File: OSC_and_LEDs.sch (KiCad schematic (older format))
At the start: 49 parts, among them Q2 IRLML2502, Q3 IRLML2502, Q4 IRLML2502, Q5 IRLML2502, Q6 IRLML2502, Q7 IRLML2502, U1 xc7a50tftg256, X1 ASFLMB

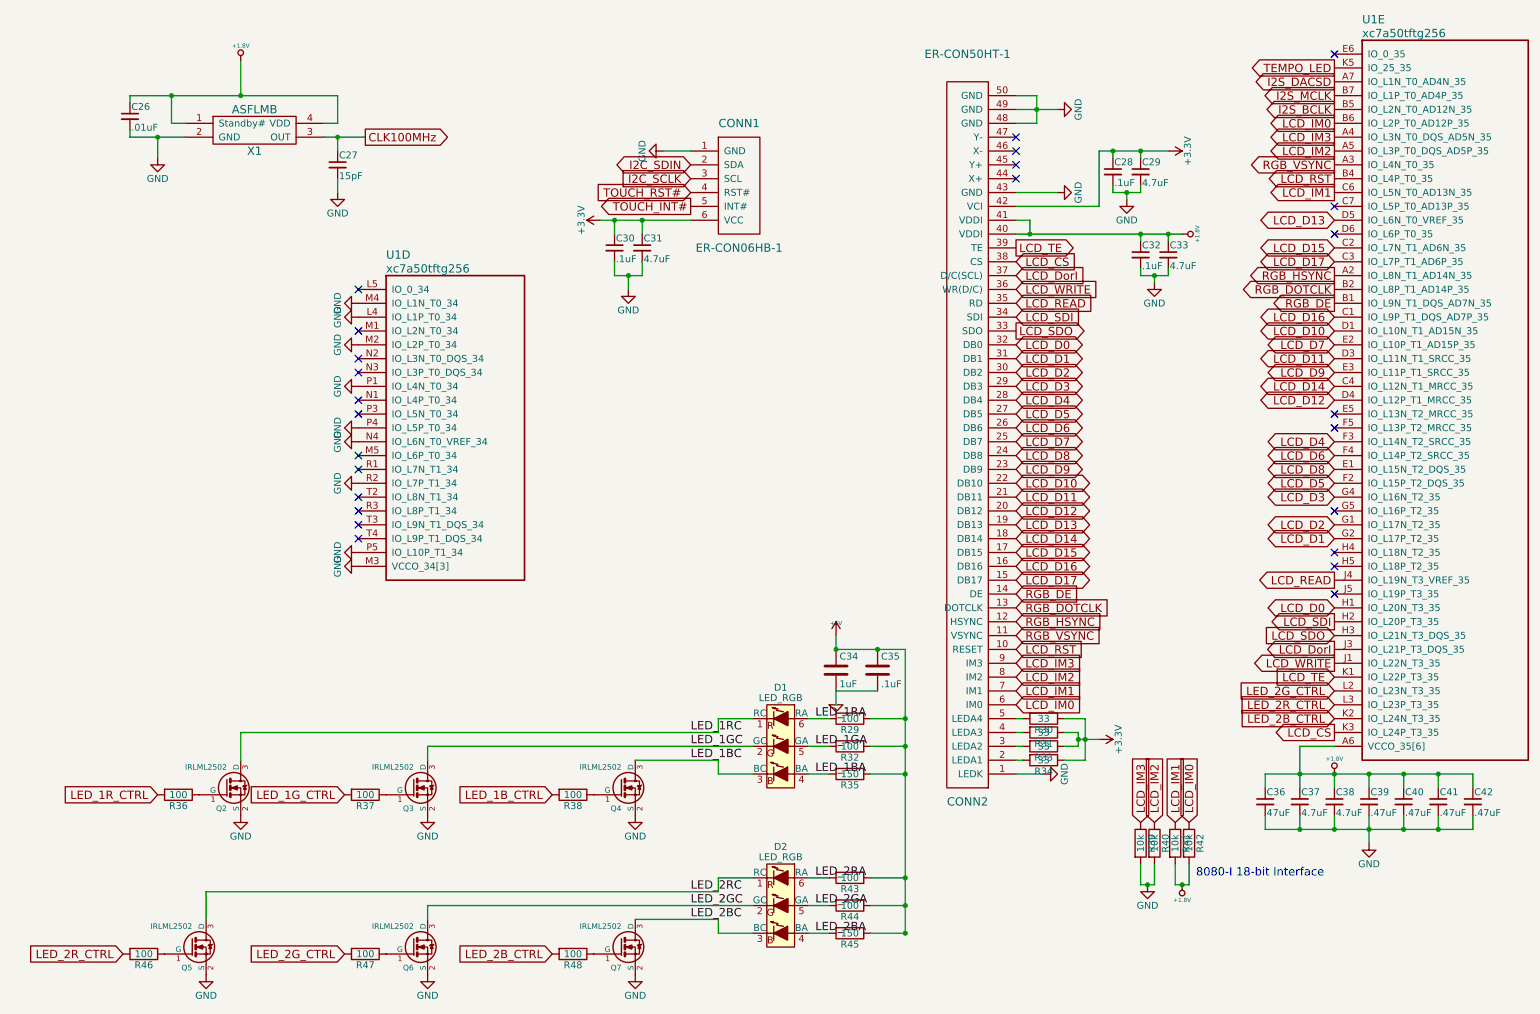
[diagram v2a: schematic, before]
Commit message: SD interface is verified and length-matched. about to increase annular ring size
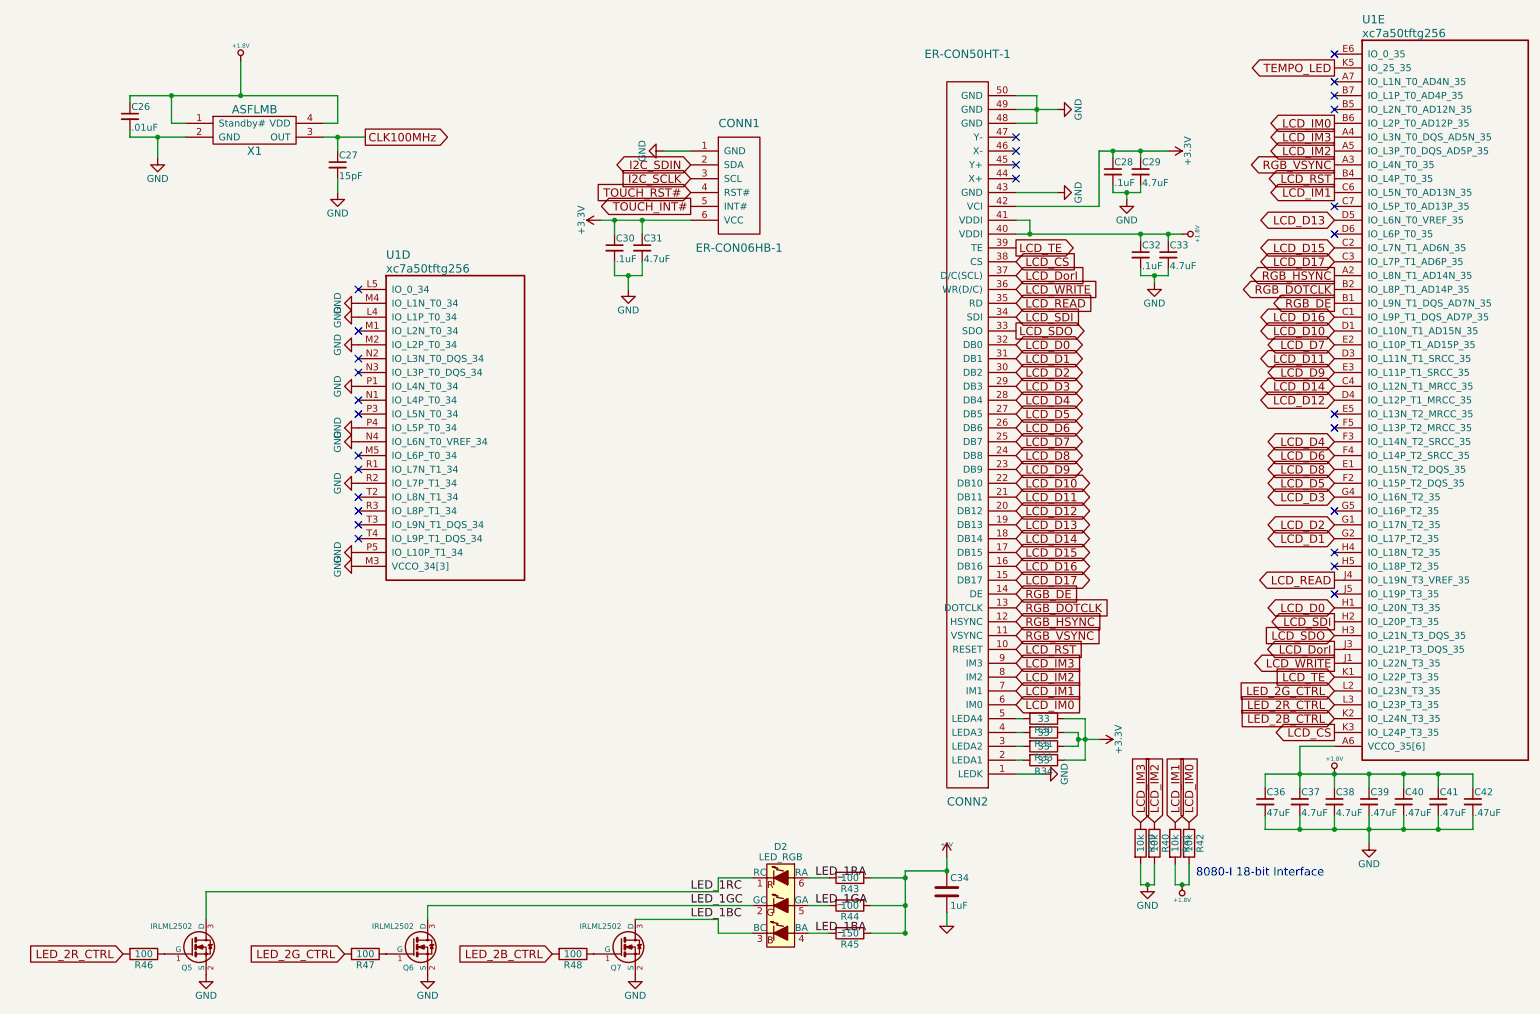
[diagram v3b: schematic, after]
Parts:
- removed C35: .1uF, Capacitors_SMD:C_0603, symbol C
- removed D1: LED_RGB, DFTcustom:PLCC6-SM-RGB-LED, symbol LED_RGB-RESCUE-DFTBoard
- removed Q2, Q3, Q4: IRLML2502, TO_SOT_Packages_SMD:SOT-23, symbol IRLML2502
- removed R29, R32, R36, R37, R38: 100, Resistors_SMD:R_0402, symbol R
- removed R35: 150, Resistors_SMD:R_0402, symbol R
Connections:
- net LED_2BA is gone; now on net LED_1BA: D2.4 (BA), R45.2
- net LED_2BC is gone; now on net LED_1BC: D2.3 (BC), Q7.3 (D)
- net LED_2GA is gone; now on net LED_1GA: D2.5 (GA), R44.2
- net LED_2GC is gone; now on net LED_1GC: D2.2 (GC), Q6.3 (D)
- net LED_2RA is gone; now on net LED_1RA: D2.6 (RA), R43.2
- net LED_2RC is gone; now on net LED_1RC: D2.1 (RC), Q5.3 (D)
- net I2S_BCLK: no longer names the net of U1.B5 (IO_L2N_T0_AD12N_35)
- net I2S_DACSD: no longer names the net of U1.A7 (IO_L1N_T0_AD4N_35)
- net I2S_MCLK: no longer names the net of U1.B7 (IO_L1P_T0_AD4P_35)
- no-connect marks 25 -> 28
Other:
- moved on the sheet: C34

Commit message: as submitted
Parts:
- C29, C31, C33, C37, C38: footprint Capacitors_SMD:C_0805 -> Capacitors_SMD:C_0603
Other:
- note added: "ER-TFT028-4"
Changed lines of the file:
@@
 F 0 "C37" H 9360 6370 50  0000 L CNN
 F 1 "4.7uF" H 9360 6220 50  0000 L CNN
-F 2 "Capacitors_SMD:C_0805" H 9350 6300 50  0001 C CNN
+F 2 "Capacitors_SMD:C_0603" H 9350 6300 50  0001 C CNN
 F 3 "" H 9350 6300 50  0001 C CNN
 F 4 "Murata" H 0   0   50  0001 C CNN "MFR"
@@
 F 0 "C38" H 9610 6370 50  0000 L CNN
 F 1 "4.7uF" H 9610 6220 50  0000 L CNN
-F 2 "Capacitors_SMD:C_0805" H 9600 6300 50  0001 C CNN
+F 2 "Capacitors_SMD:C_0603" H 9600 6300 50  0001 C CNN
 F 3 "" H 9600 6300 50  0001 C CNN
 F 4 "Murata" H 0   0   50  0001 C CNN "MFR"
@@
 $EndComp
 $Comp
-L GND #PWR52
+L GND #PWR028
 U 1 1 5908523C
 P 9850 6600
-F 0 "#PWR52" H 9850 6350 50  0001 C CNN
+F 0 "#PWR028" H 9850 6350 50  0001 C CNN
 F 1 "GND" H 9850 6450 50  0000 C CNN
 F 2 "" H 9850 6600 50  0000 C CNN
@@
 $EndComp
 $Comp
-L GND #PWR32
+L GND #PWR029
 U 1 1 59085248
 P 1100 1650
-F 0 "#PWR32" H 1100 1400 50  0001 C CNN
+F 0 "#PWR029" H 1100 1400 50  0001 C CNN
 F 1 "GND" H 1100 1500 50  0000 C CNN
 F 2 "" H 1100 1650 50  0000 C CNN
@@
 $EndComp
 $Comp
-L GND #PWR33
+L GND #PWR030
 U 1 1 59085297
 P 2400 1900
-F 0 "#PWR33" H 2400 1650 50  0001 C CNN
+F 0 "#PWR030" H 2400 1650 50  0001 C CNN
 F 1 "GND" H 2400 1750 50  0000 C CNN
 F 2 "" H 2400 1900 50  0000 C CNN
@@
 $EndComp
 $Comp
-L +5V #PWR53
+L +5V #PWR031
 U 1 1 59086616
 P 6800 6700
-F 0 "#PWR53" H 6800 6790 20  0001 C CNN
+F 0 "#PWR031" H 6800 6790 20  0001 C CNN
 F 1 "+5V" H 6800 6790 30  0000 C CNN
 F 2 "" H 6800 6700 60  0001 C CNN
@@
 $EndComp
 $Comp
-L GND-RESCUE-DFTBoard #PWR56
+L GND-RESCUE-DFTBoard #PWR032
 U 1 1 59086627
 P 6800 7200
-F 0 "#PWR56" H 6800 7200 30  0001 C CNN
+F 0 "#PWR032" H 6800 7200 30  0001 C CNN
 F 1 "GND" H 6800 7130 30  0001 C CNN
 F 2 "" H 6800 7200 60  0001 C CNN
@@
 $EndComp
 $Comp
-L GND #PWR59
+L GND #PWR033
 U 1 1 59086679
 P 4550 7550
-F 0 "#PWR59" H 4550 7300 50  0001 C CNN
+F 0 "#PWR033" H 4550 7300 50  0001 C CNN
 F 1 "GND" H 4550 7400 50  0000 C CNN
 F 2 "" H 4550 7550 50  0000 C CNN
@@
 $EndComp
 $Comp
-L GND #PWR58
+L GND #PWR034
 U 1 1 5908667F
 P 3050 7550
-F 0 "#PWR58" H 3050 7300 50  0001 C CNN
+F 0 "#PWR034" H 3050 7300 50  0001 C CNN
 F 1 "GND" H 3050 7400 50  0000 C CNN
 F 2 "" H 3050 7550 50  0000 C CNN
@@
 $EndComp
 $Comp
-L GND #PWR57
+L GND #PWR035
 U 1 1 59086685
 P 1450 7550
-F 0 "#PWR57" H 1450 7300 50  0001 C CNN
+F 0 "#PWR035" H 1450 7300 50  0001 C CNN
 F 1 "GND" H 1450 7400 50  0000 C CNN
 F 2 "" H 1450 7550 50  0000 C CNN
@@
 $EndComp
 $Comp
-L GND #PWR29
+L GND #PWR036
 U 1 1 598A88E7
 P 7600 1300
-F 0 "#PWR29" H 7600 1050 50  0001 C CNN
+F 0 "#PWR036" H 7600 1050 50  0001 C CNN
 F 1 "GND" H 7600 1150 50  0000 C CNN
 F 2 "" H 7600 1300 50  0000 C CNN
@@
 $EndComp
 $Comp
-L GND #PWR34
+L GND #PWR037
 U 1 1 598ADA0E
 P 7600 1900
-F 0 "#PWR34" H 7600 1650 50  0001 C CNN
+F 0 "#PWR037" H 7600 1650 50  0001 C CNN
 F 1 "GND" H 7600 1750 50  0000 C CNN
 F 2 "" H 7600 1900 50  0000 C CNN
@@
 $EndComp
 $Comp
-L GND #PWR50
+L GND #PWR038
 U 1 1 598B6836
 P 7500 6100
-F 0 "#PWR50" H 7500 5850 50  0001 C CNN
+F 0 "#PWR038" H 7500 5850 50  0001 C CNN
 F 1 "GND" H 7500 5950 50  0000 C CNN
 F 2 "" H 7500 6100 50  0000 C CNN
@@
 $EndComp
 $Comp
-L +1.8V #PWR28
+L +1.8V #PWR039
 U 1 1 598B5F68
 P 1700 950
-F 0 "#PWR28" H 1700 1090 20  0001 C CNN
+F 0 "#PWR039" H 1700 1090 20  0001 C CNN
 F 1 "+1.8V" H 1700 1060 30  0000 C CNN
 F 2 "" H 1700 950 60  0001 C CNN
@@
 $EndComp
 $Comp
-L +1.8V #PWR51
+L +1.8V #PWR040
 U 1 1 598B6CF5
 P 9600 6100
-F 0 "#PWR51" H 9600 6240 20  0001 C CNN
+F 0 "#PWR040" H 9600 6240 20  0001 C CNN
 F 1 "+1.8V" H 9600 6210 30  0000 C CNN
 F 2 "" H 9600 6100 60  0001 C CNN
@@
 $EndComp
 $Comp
-L +3.3V #PWR31
+L +3.3V #PWR041
 U 1 1 598B98DD
 P 8400 1600
-F 0 "#PWR31" H 8400 1450 50  0001 C CNN
+F 0 "#PWR041" H 8400 1450 50  0001 C CNN
 F 1 "+3.3V" H 8400 1740 50  0000 C CNN
 F 2 "" H 8400 1600 50  0000 C CNN
@@
 $EndComp
 $Comp
-L +1.8V #PWR37
+L +1.8V #PWR042
 U 1 1 598BA87D
 P 8500 2200
-F 0 "#PWR37" H 8500 2340 20  0001 C CNN
+F 0 "#PWR042" H 8500 2340 20  0001 C CNN
 F 1 "+1.8V" H 8500 2310 30  0000 C CNN
 F 2 "" H 8500 2200 60  0001 C CNN
@@
 F 0 "C29" H 8210 1820 50  0000 L CNN
 F 1 "4.7uF" H 8210 1670 50  0000 L CNN
-F 2 "Capacitors_SMD:C_0805" H 8200 1750 50  0001 C CNN
+F 2 "Capacitors_SMD:C_0603" H 8200 1750 50  0001 C CNN
 F 3 "" H 8200 1750 50  0001 C CNN
 F 4 "Murata" H 0   0   50  0001 C CNN "MFR"
@@
 F 0 "C33" H 8410 2420 50  0000 L CNN
 F 1 "4.7uF" H 8410 2270 50  0000 L CNN
-F 2 "Capacitors_SMD:C_0805" H 8400 2350 50  0001 C CNN
+F 2 "Capacitors_SMD:C_0603" H 8400 2350 50  0001 C CNN
 F 3 "" H 8400 2350 50  0001 C CNN
 F 4 "Murata" H 0   0   50  0001 C CNN "MFR"
@@
 $EndComp
 $Comp
-L GND #PWR35
+L GND #PWR043
 U 1 1 598BEE0D
 P 8100 1950
-F 0 "#PWR35" H 8100 1700 50  0001 C CNN
+F 0 "#PWR043" H 8100 1700 50  0001 C CNN
 F 1 "GND" H 8100 1800 50  0000 C CNN
 F 2 "" H 8100 1950 50  0000 C CNN
@@
 $EndComp
 $Comp
-L GND #PWR38
+L GND #PWR044
 U 1 1 598BEE7B
 P 8300 2550
-F 0 "#PWR38" H 8300 2300 50  0001 C CNN
+F 0 "#PWR044" H 8300 2300 50  0001 C CNN
 F 1 "GND" H 8300 2400 50  0000 C CNN
 F 2 "" H 8300 2550 50  0000 C CNN
@@
 $EndComp
 $Comp
-L +3.3V #PWR49
+L +3.3V #PWR045
 U 1 1 598CDBCB
 P 7900 5850
-F 0 "#PWR49" H 7900 5700 50  0001 C CNN
+F 0 "#PWR045" H 7900 5700 50  0001 C CNN
 F 1 "+3.3V" H 7900 5990 50  0000 C CNN
 F 2 "" H 7900 5850 50  0000 C CNN
@@
 $EndComp
 $Comp
-L GND #PWR30
+L GND #PWR046
 U 1 1 598F040F
 P 4750 1600
-F 0 "#PWR30" H 4750 1350 50  0001 C CNN
+F 0 "#PWR046" H 4750 1350 50  0001 C CNN
 F 1 "GND" H 4750 1450 50  0000 C CNN
 F 2 "" H 4750 1600 50  0000 C CNN
@@
 $EndComp
 $Comp
-L +3.3V #PWR36
+L +3.3V #PWR047
 U 1 1 598F1F44
 P 4300 2100
-F 0 "#PWR36" H 4300 1950 50  0001 C CNN
+F 0 "#PWR047" H 4300 1950 50  0001 C CNN
 F 1 "+3.3V" H 4300 2240 50  0000 C CNN
 F 2 "" H 4300 2100 50  0000 C CNN
@@
 F 0 "C31" H 4610 2370 50  0000 L CNN
 F 1 "4.7uF" H 4610 2220 50  0000 L CNN
-F 2 "Capacitors_SMD:C_0805" H 4600 2300 50  0001 C CNN
+F 2 "Capacitors_SMD:C_0603" H 4600 2300 50  0001 C CNN
 F 3 "" H 4600 2300 50  0001 C CNN
 F 4 "Murata" H 0   0   50  0001 C CNN "MFR"
@@
 $EndComp
 $Comp
-L GND #PWR39
+L GND #PWR048
 U 1 1 598FDD2A
 P 4500 2600
-F 0 "#PWR39" H 4500 2350 50  0001 C CNN
+F 0 "#PWR048" H 4500 2350 50  0001 C CNN
 F 1 "GND" H 4500 2450 50  0000 C CNN
 F 2 "" H 4500 2600 50  0000 C CNN
@@
 $EndComp
 $Comp
-L GND #PWR47
+L GND #PWR049
 U 1 1 598D6E85
 P 2550 4500
-F 0 "#PWR47" H 2550 4250 50  0001 C CNN
+F 0 "#PWR049" H 2550 4250 50  0001 C CNN
 F 1 "GND" H 2550 4350 50  0000 C CNN
 F 2 "" H 2550 4500 50  0000 C CNN
@@
 $EndComp
 $Comp
-L GND #PWR46
+L GND #PWR050
 U 1 1 598D6E8B
 P 2550 4000
-F 0 "#PWR46" H 2550 3750 50  0001 C CNN
+F 0 "#PWR050" H 2550 3750 50  0001 C CNN
 F 1 "GND" H 2550 3850 50  0000 C CNN
 F 2 "" H 2550 4000 50  0000 C CNN
@@
 $EndComp
 $Comp
-L GND #PWR45
+L GND #PWR051
 U 1 1 598D6E97
 P 2550 3700
-F 0 "#PWR45" H 2550 3450 50  0001 C CNN
+F 0 "#PWR051" H 2550 3450 50  0001 C CNN
 F 1 "GND" H 2550 3550 50  0000 C CNN
 F 2 "" H 2550 3700 50  0000 C CNN
@@
 $EndComp
 $Comp
-L GND #PWR44
+L GND #PWR052
 U 1 1 598D6E9D
 P 2550 3600
-F 0 "#PWR44" H 2550 3350 50  0001 C CNN
+F 0 "#PWR052" H 2550 3350 50  0001 C CNN
 F 1 "GND" H 2550 3450 50  0000 C CNN
 F 2 "" H 2550 3600 50  0000 C CNN
@@
 $EndComp
 $Comp
-L GND #PWR43
+L GND #PWR053
 U 1 1 598D6EA3
 P 2550 3300
-F 0 "#PWR43" H 2550 3050 50  0001 C CNN
+F 0 "#PWR053" H 2550 3050 50  0001 C CNN
 F 1 "GND" H 2550 3150 50  0000 C CNN
 F 2 "" H 2550 3300 50  0000 C CNN
@@
 $EndComp
 $Comp
-L GND #PWR42
+L GND #PWR054
 U 1 1 598D6EA9
 P 2550 3000
-F 0 "#PWR42" H 2550 2750 50  0001 C CNN
+F 0 "#PWR054" H 2550 2750 50  0001 C CNN
 F 1 "GND" H 2550 2850 50  0000 C CNN
 F 2 "" H 2550 3000 50  0000 C CNN
@@
 $EndComp
 $Comp
-L GND #PWR40
+L GND #PWR055
 U 1 1 598D6EAF
 P 2550 2700
-F 0 "#PWR40" H 2550 2450 50  0001 C CNN
+F 0 "#PWR055" H 2550 2450 50  0001 C CNN
 F 1 "GND" H 2550 2550 50  0000 C CNN
 F 2 "" H 2550 2700 50  0000 C CNN
@@
 $EndComp
 $Comp
-L GND #PWR41
+L GND #PWR056
 U 1 1 598D6EB7
 P 2550 2800
-F 0 "#PWR41" H 2550 2550 50  0001 C CNN
+F 0 "#PWR056" H 2550 2550 50  0001 C CNN
 F 1 "GND" H 2550 2650 50  0000 C CNN
 F 2 "" H 2550 2800 50  0000 C CNN
@@
 $EndComp
 $Comp
-L +1.8V #PWR55
+L +1.8V #PWR057
 U 1 1 598CFD34
 P 8500 6900
-F 0 "#PWR55" H 8500 7040 20  0001 C CNN
+F 0 "#PWR057" H 8500 7040 20  0001 C CNN
 F 1 "+1.8V" H 8500 7010 30  0000 C CNN
 F 2 "" H 8500 6900 60  0001 C CNN
@@
 $EndComp
 $Comp
-L GND #PWR54
+L GND #PWR058
 U 1 1 598D049B
 P 8250 6900
-F 0 "#PWR54" H 8250 6650 50  0001 C CNN
+F 0 "#PWR058" H 8250 6650 50  0001 C CNN
 F 1 "GND" H 8250 6750 50  0000 C CNN
 F 2 "" H 8250 6900 50  0000 C CNN
@@
 $EndComp
 $Comp
-L GND #PWR48
+L GND #PWR059
 U 1 1 5A746D29
 P 2550 4600
-F 0 "#PWR48" H 2550 4350 50  0001 C CNN
+F 0 "#PWR059" H 2550 4350 50  0001 C CNN
 F 1 "GND" H 2550 4450 50  0000 C CNN
 F 2 "" H 2550 4600 50  0000 C CNN
@@
 NoConn ~ 9600 1200
 NoConn ~ 9600 1300
+Text Notes 7800 5450 0    60   ~ 0
+ER-TFT028-4
 $EndSCHEMATC

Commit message: boutta merge
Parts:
- C26, C27, C28, C29, C30, C31, C32, C33, C36, C37, C38, C39, C40, C41, C42: symbol C_Small -> DFTBoard-rescue:C_Small
- C34: symbol C -> DFTBoard-rescue:C
- CONN1: symbol ER-CON06HB-1 -> DFTBoard-rescue:ER-CON06HB-1
- CONN2: symbol ER-CON50HT-1 -> DFTBoard-rescue:ER-CON50HT-1
- D2: symbol LED_RGB-RESCUE-DFTBoard -> DFTBoard-rescue:LED_RGB-RESCUE-DFTBoard
- Q5, Q6, Q7: symbol IRLML2502 -> DFTBoard-rescue:IRLML2502
- R30, R31, R33, R34, R39, R40, R41, R42, R43, R44, R45, R46, R47, R48: symbol R -> DFTBoard-rescue:R
- U1: symbol xc7a50tftg256 -> DFTBoard-rescue:xc7a50tftg256
- X1: symbol ASFLMB -> DFTBoard-rescue:ASFLMB
